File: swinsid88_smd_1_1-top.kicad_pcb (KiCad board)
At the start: 2 copper layers, 17.8 x 38.3 mm, 15 parts, among them J1 6581, U1 ATmega88PA-A, U3 Program, U5 ASDMB-32MHz

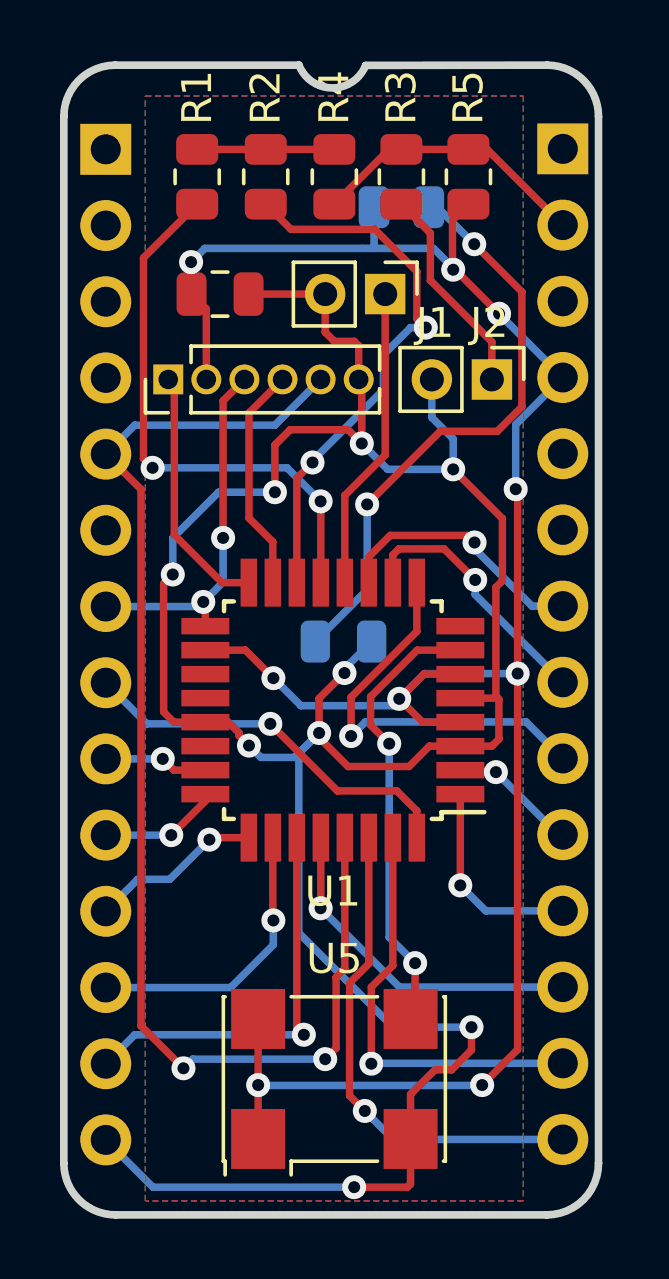
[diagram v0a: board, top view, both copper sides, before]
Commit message: chore: improve groundplane
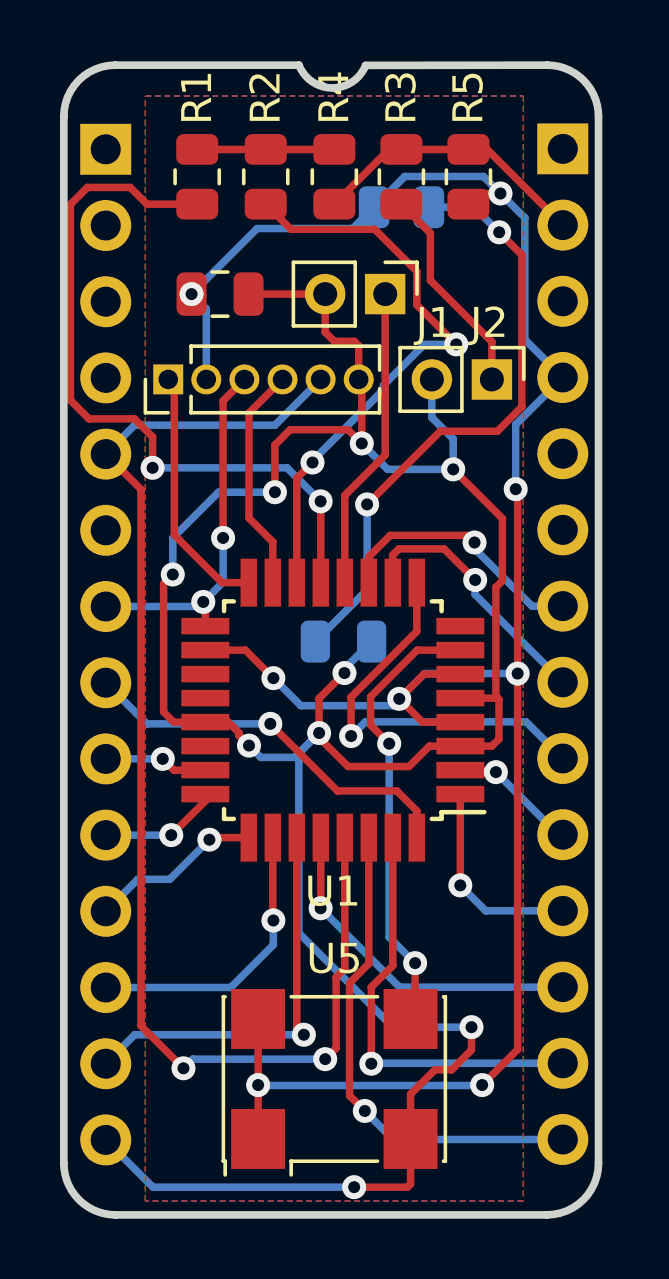
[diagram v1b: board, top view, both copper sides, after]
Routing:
- net AUD1: track 18.4 -> 24.3 mm
- net AUD2: track 18.5 -> 19.7 mm
- net +V: track 74.8 -> 76.0 mm, vias 9 -> 8
- net Net-(D1-A): track 19.9 -> 20.6 mm

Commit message: feature: hide components
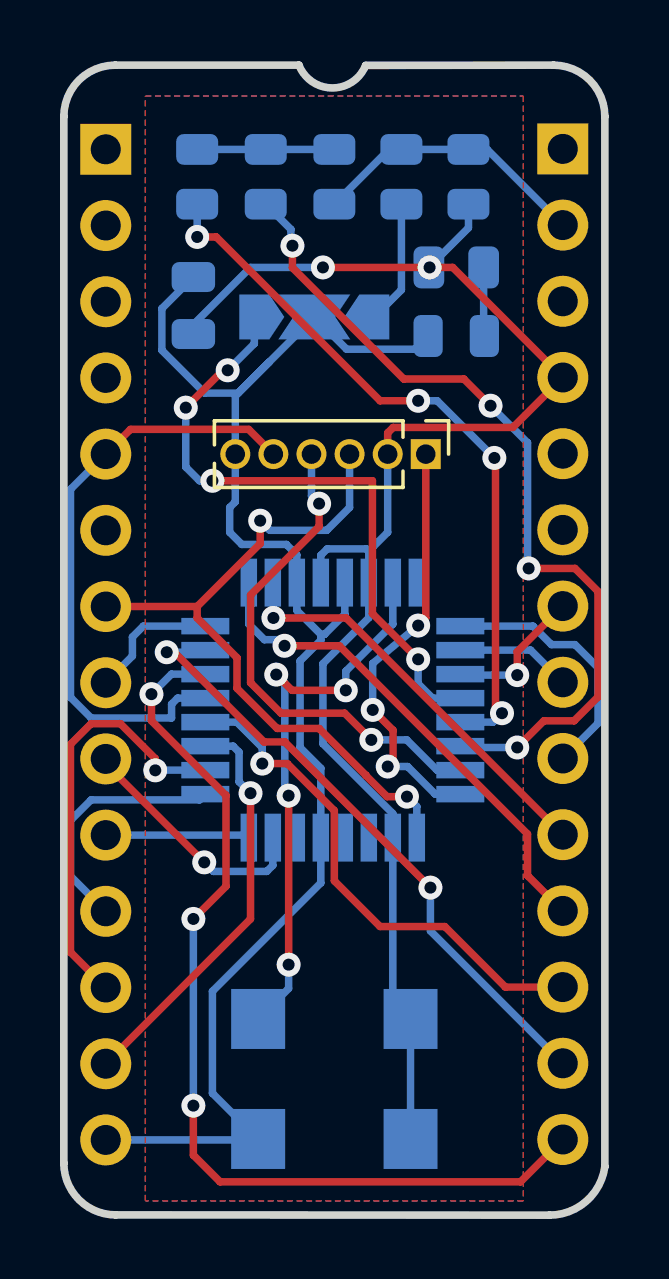
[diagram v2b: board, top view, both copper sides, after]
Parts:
- removed J2: ~, Connector_PinHeader_2.00mm:PinHeader_1x02_P2.00mm_Vertical
- C1, R1, R2, R3, R4, R5, U1, U5: moved to B.Cu
- J1: value 6581 -> 6581/8580; footprint Connector_PinHeader_2.00mm:PinHeader_1x02_P2.00mm_Vertical -> Jumper:SolderJumper-3_P2.0mm_Open_TrianglePad1.0x1.5mm; moved to B.Cu
- moved D1 10.9 mm to (145.8, 83.0), turned to 0 degrees
- moved U3 8.94 mm to (144.8, 86.9), turned to -90 degrees
- moved R6 2.71 mm to (145.8, 80.7)
- moved J1 2.48 mm to (141.1, 82.3), turned to 180 degrees
- moved C1 0.97 mm to (137.1, 82.0), turned to 90 degrees
- turned U1 to -90 degrees
- turned U5 to 180 degrees
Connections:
- J1 pad 1: 6581Sel -> Net-(J1-Pin_1)
- R3 pad 2: Net-(J2-Pin_1) -> Net-(J1-Pin_1)
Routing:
- net GND: track 89.2 -> 52.5 mm, vias 9 -> 0
- net +V: track 76.0 -> 52.4 mm, vias 8 -> 2
- net ~{RESET}: track 42.2 -> 20.2 mm, vias 2 -> 0
- net Net-(D1-A): track 20.6 -> 2.30 mm, vias 2 -> 0
- net D0: track 16.6 -> 32.2 mm, vias 1 -> 3
- net SCK: track 12.1 -> 23.9 mm
- net 6581Sel: track 10.2 -> 21.5 mm, vias 0 -> 4
- net D3: track 6.81 -> 16.6 mm
- net D4: track 4.31 -> 13.8 mm
- net MOSI: track 7.57 -> 16.9 mm, vias 0 -> 2
- net AUD2: track 19.7 -> 28.4 mm, vias 2 -> 4
- net ~{CS}: track 13.0 -> 4.47 mm, vias 1 -> 0
- net Net-(J2-Pin_1): track 7.09 -> 0.00 mm
- net D1: track 14.2 -> 21.0 mm, vias 1 -> 2
- net MISO: track 8.41 -> 14.4 mm, vias 0 -> 3
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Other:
- board size 17.8 x 38.3 mm -> 18 x 38.3 mm

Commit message: prettify board
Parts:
- added G***: LOGO, sid:MOS, F.Cu at (145.6, 93.3)
- J1: footprint Jumper:SolderJumper-3_P2.0mm_Open_TrianglePad1.0x1.5mm -> Jumper:SolderJumper-3_P1.3mm_Bridged12_Pad1.0x1.5mm
- U3: moved to B.Cu
- turned J1 to 0 degrees
- turned U3 to 90 degrees
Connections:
- J1 pad 1: Net-(J1-Pin_1) -> 6581Sel
- J1 pad 3: 6581Sel -> Net-(J1-Pin_3)
- R3 pad 2: Net-(J1-Pin_1) -> Net-(J1-Pin_3)
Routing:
- net GND: track 52.5 -> 57.3 mm
- net Net-(J1-Pin_3): track 0.00 -> 4.42 mm
- net Net-(J1-Pin_1): track 4.13 -> 0.00 mm
- net SCK: track 23.9 -> 25.4 mm
- net +V: track 52.4 -> 53.0 mm
- net D1: vias 2 -> 3
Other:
- board text added: "- nano SwinSID b -"
- board text added: "0923"
- board text added: "6581 CBM"

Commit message: update component details
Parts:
- C1: value C_Small -> 0.1uF
- U1: value ATmega88PA-A -> ATmega88PA-AU
- U5: value ASDMB-32MHz -> CB3-3C-32M000000
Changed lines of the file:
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@@
     (descr "Resistor SMD 0805 (2012 Metric), square (rectangular) end terminal, IPC_7351 nominal, (Body size source: IPC-SM-782 page 72, https://www.pcb-3d.com/wordpress/wp-content/uploads/ipc-sm-782a_amendment_1_and_2.pdf), generated with kicad-footprint-generator")
     (tags "resistor")
+    (property "Digikey" "RMCF0805FT240KCT-ND")
     (property "Sheetfile" "swinsid88_smd_1_1-top.kicad_sch")
     (property "Sheetname" "")
@@
     (descr "Capacitor SMD 0805 (2012 Metric), square (rectangular) end terminal, IPC_7351 nominal, (Body size source: IPC-SM-782 page 76, https://www.pcb-3d.com/wordpress/wp-content/uploads/ipc-sm-782a_amendment_1_and_2.pdf, https://docs.google.com/spreadsheets/d/1BsfQQcO9C6DZCsRaXUlFlo91Tg2WpOkGARC1WS5S8t0/edit?usp=sharing), generated with kicad-footprint-generator")
     (tags "capacitor")
+    (property "Digikey" "1276-1003-1-ND")
     (property "Sheetfile" "swinsid88_smd_1_1-top.kicad_sch")
     (property "Sheetname" "")
@@
         (effects (font (size 1 1) (thickness 0.15)) (justify mirror))
     )
-    (fp_text value "C_Small" (at 0 -1.68 90) (layer "B.Fab") hide
+    (fp_text value "0.1uF" (at 0 -1.68 90) (layer "B.Fab") hide
         (effects (font (size 1 1) (thickness 0.15)) (justify mirror))
     )
@@
     (descr "Resistor SMD 0805 (2012 Metric), square (rectangular) end terminal, IPC_7351 nominal, (Body size source: IPC-SM-782 page 72, https://www.pcb-3d.com/wordpress/wp-content/uploads/ipc-sm-782a_amendment_1_and_2.pdf), generated with kicad-footprint-generator")
     (tags "resistor")
+    (property "Digikey" "RMCF0805FT2K20CT-ND")
     (property "Sheetfile" "swinsid88_smd_1_1-top.kicad_sch")
     (property "Sheetname" "")
@@
     (descr "Resistor SMD 0805 (2012 Metric), square (rectangular) end terminal, IPC_7351 nominal, (Body size source: IPC-SM-782 page 72, https://www.pcb-3d.com/wordpress/wp-content/uploads/ipc-sm-782a_amendment_1_and_2.pdf), generated with kicad-footprint-generator")
     (tags "resistor")
+    (property "Digikey" "RNCP0805FTD1K00CT-ND")
     (property "Sheetfile" "swinsid88_smd_1_1-top.kicad_sch")
     (property "Sheetname" "")
@@
     (descr "32-Lead Plastic Thin Quad Flatpack (PT) - 7x7x1.0 mm Body, 2.00 mm [TQFP] (see Microchip Packaging Specification 00000049BS.pdf)")
     (tags "QFP 0.8")
+    (property "Digikey" "ATMEGA88PA-AU-ND")
     (property "Sheetfile" "swinsid88_smd_1_1-top.kicad_sch")
     (property "Sheetname" "")
@@
         (effects (font (size 1 1) (thickness 0.15)) (justify mirror))
     )
-    (fp_text value "ATmega88PA-A" (at 0 -6.05 90) (layer "B.Fab") hide
+    (fp_text value "ATmega88PA-AU" (at 0 -6.05 90) (layer "B.Fab") hide
         (effects (font (size 1 1) (thickness 0.15)) (justify mirror))
     )
@@
     (descr "Diode SMD 0805 (2012 Metric), square (rectangular) end terminal, IPC_7351 nominal, (Body size source: https://docs.google.com/spreadsheets/d/1BsfQQcO9C6DZCsRaXUlFlo91Tg2WpOkGARC1WS5S8t0/edit?usp=sharing), generated with kicad-footprint-generator")
     (tags "diode")
+    (property "Digikey" "732-4987-1-ND")
     (property "Sheetfile" "swinsid88_smd_1_1-top.kicad_sch")
     (property "Sheetname" "")
@@
     (descr "Resistor SMD 0805 (2012 Metric), square (rectangular) end terminal, IPC_7351 nominal, (Body size source: IPC-SM-782 page 72, https://www.pcb-3d.com/wordpress/wp-content/uploads/ipc-sm-782a_amendment_1_and_2.pdf), generated with kicad-footprint-generator")
     (tags "resistor")
+    (property "Digikey" "RNCP0805FTD1K00CT-ND")
     (property "Sheetfile" "swinsid88_smd_1_1-top.kicad_sch")
     (property "Sheetname" "")
@@
     (descr "Resistor SMD 0805 (2012 Metric), square (rectangular) end terminal, IPC_7351 nominal, (Body size source: IPC-SM-782 page 72, https://www.pcb-3d.com/wordpress/wp-content/uploads/ipc-sm-782a_amendment_1_and_2.pdf), generated with kicad-footprint-generator")
     (tags "resistor")
+    (property "Digikey" "RMCF0805FT330RCT-ND")
     (property "Sheetfile" "swinsid88_smd_1_1-top.kicad_sch")
     (property "Sheetname" "")
@@
     (descr "Miniature Crystal Clock Oscillator Abracon ASV series, http://www.abracon.com/Oscillators/ASV.pdf, 7.0x5.1mm^2 package")
     (tags "SMD SMT crystal oscillator")
+    (property "Digikey" "110-CB3-3C-32M000000CT-ND")
     (property "Sheetfile" "swinsid88_smd_1_1-top.kicad_sch")
     (property "Sheetname" "")
@@
         (effects (font (size 1 1) (thickness 0.15)) (justify mirror))
     )
-    (fp_text value "ASDMB-32MHz" (at 0 -4) (layer "B.Fab") hide
+    (fp_text value "CB3-3C-32M000000" (at 0 -4) (layer "B.Fab") hide
         (effects (font (size 1 1) (thickness 0.15)) (justify mirror))
     )
@@
     (descr "Resistor SMD 0805 (2012 Metric), square (rectangular) end terminal, IPC_7351 nominal, (Body size source: IPC-SM-782 page 72, https://www.pcb-3d.com/wordpress/wp-content/uploads/ipc-sm-782a_amendment_1_and_2.pdf), generated with kicad-footprint-generator")
     (tags "resistor")
-    (property "Sheetfile" "swinsid88_smd_1_1-top.kicad_sch")
-    (property "Sheetname" "")
+    (property "Digikey" "RMCF0805FT4K70CT-ND")
+    (property "Sheetfile" "swinsid88_smd_1_1-top.kicad_sch")
+    (property "Sheetname" "")

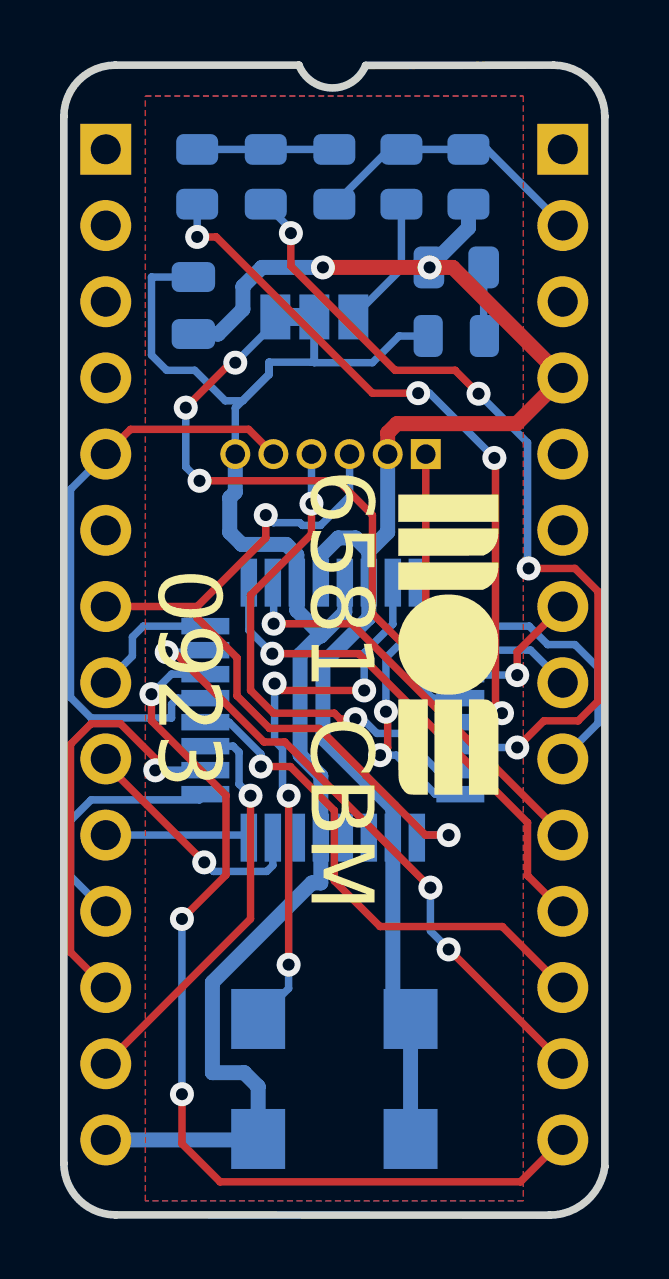
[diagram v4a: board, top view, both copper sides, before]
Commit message: use handsolder footprints
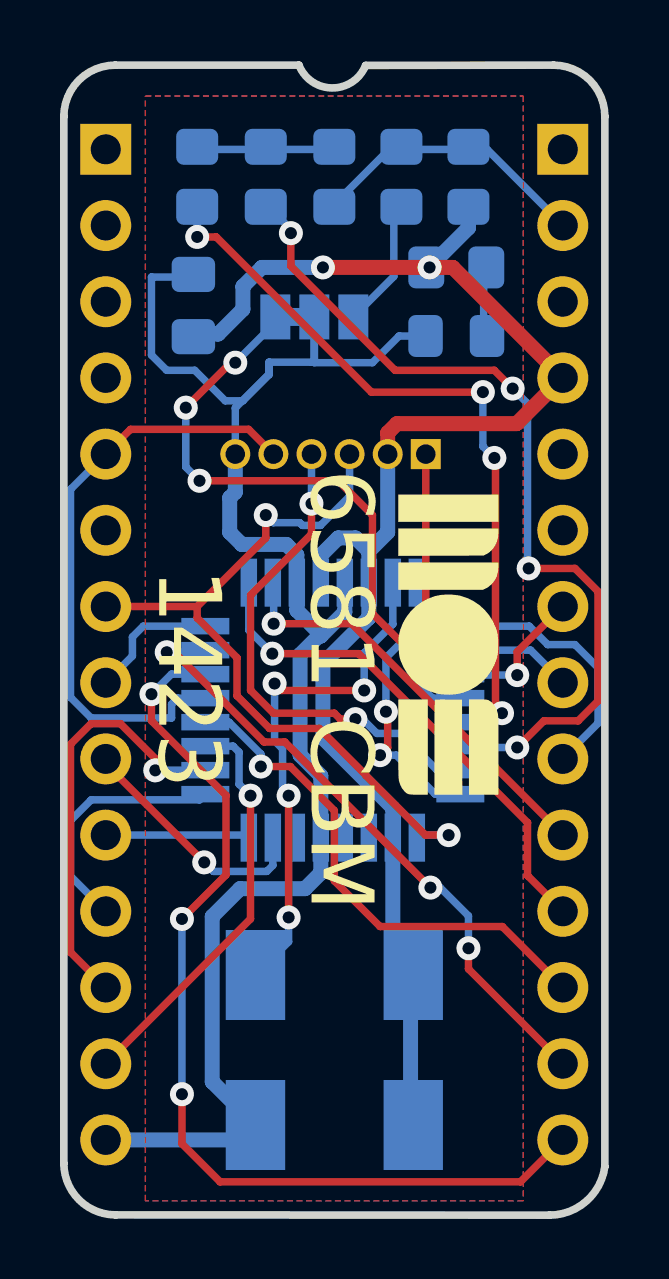
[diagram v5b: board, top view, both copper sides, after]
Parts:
- C1: footprint Capacitor_SMD:C_0805_2012Metric -> Capacitor_SMD:C_0805_2012Metric_Pad1.18x1.45mm_HandSolder
- D1: footprint Diode_SMD:D_0805_2012Metric -> Diode_SMD:D_0805_2012Metric_Pad1.15x1.40mm_HandSolder
- R1, R2, R3, R4, R5, R6: footprint Resistor_SMD:R_0805_2012Metric -> Resistor_SMD:R_0805_2012Metric_Pad1.20x1.40mm_HandSolder
- U5: footprint Oscillator:Oscillator_SMD_Abracon_ASV-4Pin_7.0x5.1mm -> Oscillator:Oscillator_SMD_Abracon_ASV-4Pin_7.0x5.1mm_HandSoldering
- moved U5 0.97 mm to (141.8, 106.8)
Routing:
- net PB6: track 18.9 -> 17.3 mm
- net AUD1: track 24.2 -> 25.2 mm
- net AUD2: track 28.5 -> 29.2 mm
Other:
- board text added: "."
- board text added: "1423"
- board text removed: "0923"
